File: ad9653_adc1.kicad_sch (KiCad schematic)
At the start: 20 parts, among them J701 142-0701-201, J702 142-0701-201, J703 142-0701-201, J704 142-0701-201, U701 AD9653BCPZ-125

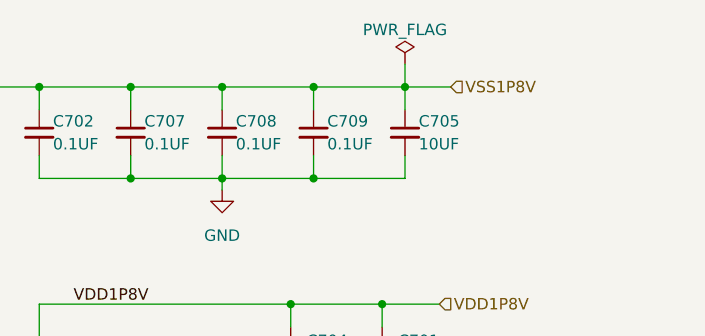
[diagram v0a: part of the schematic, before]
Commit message: resolve duplicate power flag
kicad 8 complains about two power flags on VSS1P8V net,
one each on ADC0 and ADC1 pages.  Consolidate to one
flag on the U35_LT6233 page.
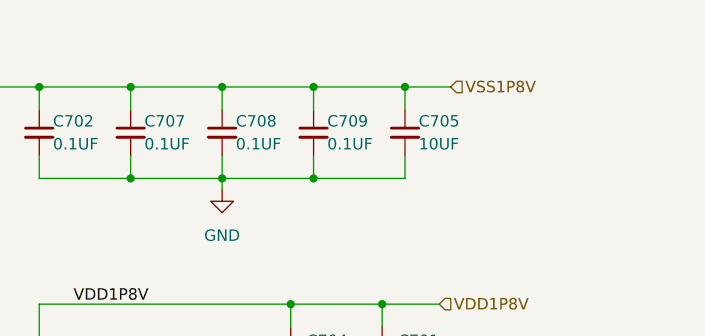
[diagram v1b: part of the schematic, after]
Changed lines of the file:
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@@
-	(wire
-		(pts
-			(xy 271.78 73.66) (xy 271.78 76.2)
-		)
-		(stroke
-			(width 0)
-			(type default)
-		)
-	)
 	(wire
 		(pts
@@
 					(unit 1)
 				)
-			)
-		)
-	)
-	(symbol
-		(lib_id "power:PWR_FLAG")
-		(at 271.78 73.66 0)
-		(mirror y)
-		(unit 1)
-		(exclude_from_sim no)
-		(in_bom yes)
-		(on_board yes)
-		(dnp no)
-		(property "Reference" "#FLG05"
-			(at 271.78 71.755 0)
-			(effects
-				(font
-					(size 1.27 1.27)
-				)
-				(hide yes)
-			)
-		)
-		(property "Value" "PWR_FLAG"
-			(at 271.78 69.85 0)
-			(effects
-				(font
-					(size 1.27 1.27)
-				)
-			)
-		)
-		(property "Footprint" ""
-			(at 271.78 73.66 0)
-			(effects
-				(font
-					(size 1.27 1.27)
-				)
-				(hide yes)
-			)
-		)
-		(property "Datasheet" "~"
-			(at 271.78 73.66 0)
-			(effects
-				(font
-					(size 1.27 1.27)
-				)
-				(hide yes)
-			)
-		)
-		(property "Description" "Special symbol for telling ERC where power comes from"
-			(at 271.78 73.66 0)
-			(effects
-				(font
-					(size 1.27 1.27)
-				)
-				(hide yes)
-			)
-		)
-		(pin "1"
-		)
-		(instances
-			(project "zest"
-				(path "/00000000-0000-0000-0000-000000000003/00000000-0000-0000-0000-000000000001"
-					(reference "#FLG05")
-					(unit 1)
-				)
